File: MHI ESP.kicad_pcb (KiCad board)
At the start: 2 copper layers, 26 x 59.2 mm, 22 parts, among them J1 CNS, J2 DISPLAY, J3 Conn_01x01_Male, Q1 BSS138, Q2 BSS138, Q3 BSS138, Q4 BSS138, Q5 BSS138, U1 WeMos_D1_mini, U2 LD1117S50TR

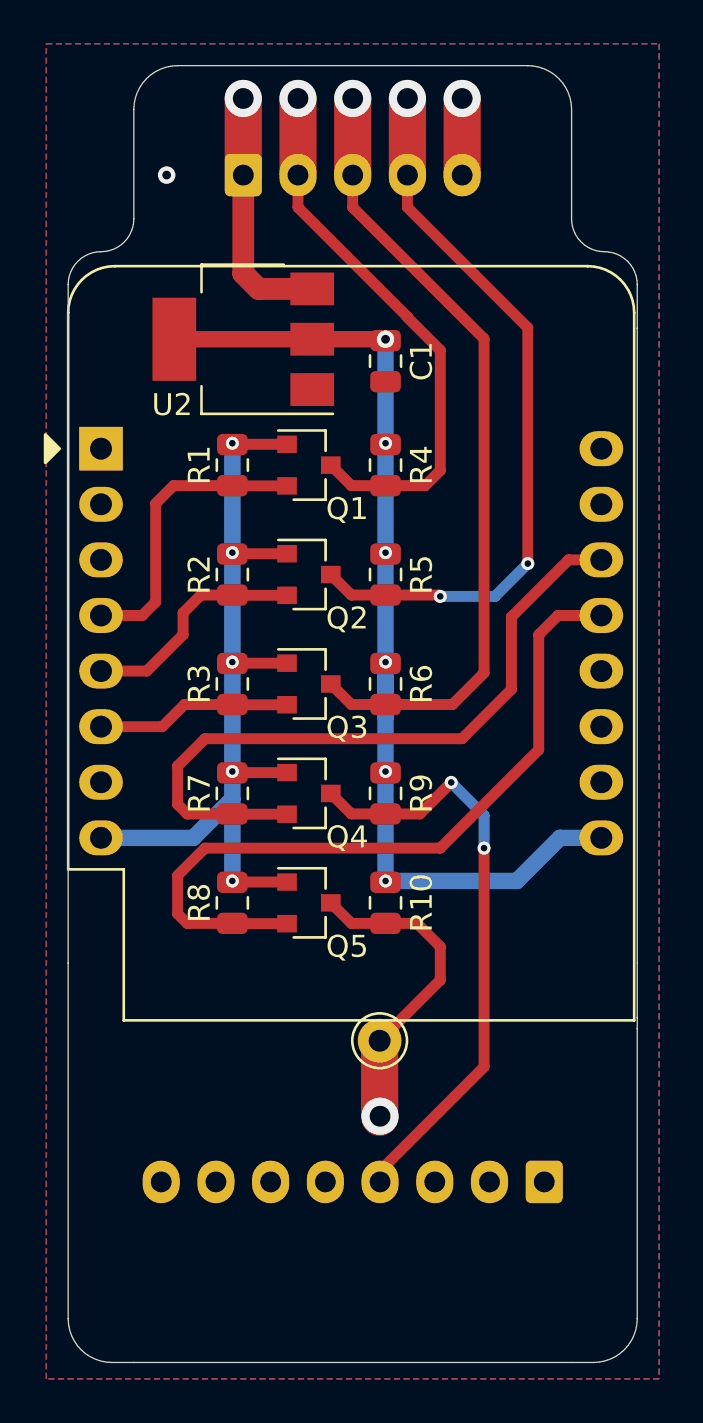
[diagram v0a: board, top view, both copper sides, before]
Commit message: Updated to v4.0
Added WAGO terminals for IR signal in and out.
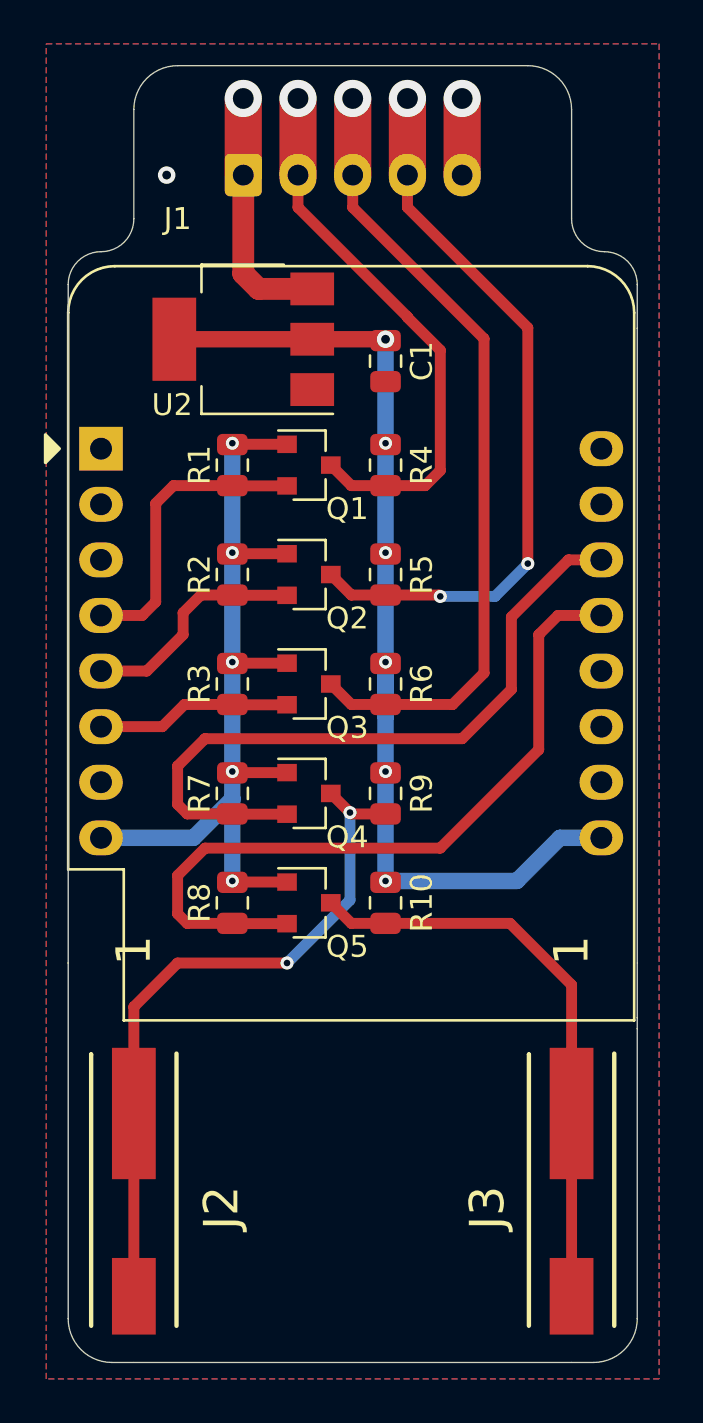
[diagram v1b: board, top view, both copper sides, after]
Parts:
- J2: value DISPLAY -> 2060-451/998-404; footprint Connector_JST:JST_XH_S8B-XH-A-1_1x08_P2.50mm_Horizontal -> wago:P-2060-451_998-404; moved to F.Cu
- J3: value Conn_01x01_Male -> 2060-451/998-404; footprint Connector_Pin:Pin_D1.0mm_L10.0mm -> wago:P-2060-451_998-404
- moved J2 18.8 mm to (115.0, 127.0), turned to 90 degrees
- moved J3 11.5 mm to (135.0, 127.0), turned to 90 degrees
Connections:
- U1 pad 1: (no net) -> unconnected-(U1-Pad1)
- U1 pad 11: (no net) -> unconnected-(U1-Pad11)
- U1 pad 12: (no net) -> unconnected-(U1-Pad12)
- U1 pad 15: (no net) -> unconnected-(U1-Pad15)
- U1 pad 16: (no net) -> unconnected-(U1-Pad16)
- U1 pad 2: (no net) -> unconnected-(U1-Pad2)
- U1 pad 3: (no net) -> unconnected-(U1-Pad3)
- U1 pad 7: (no net) -> unconnected-(U1-Pad7)
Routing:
- net IRDOUT: track 14.8 -> 26.8 mm, vias 1 -> 0
- net IRDIN: track 27.3 -> 32.0 mm
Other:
- net class Default removed
- board text added: "AC-WiFi v4.0"
- board text removed: "AC-WiFi v3.0"
